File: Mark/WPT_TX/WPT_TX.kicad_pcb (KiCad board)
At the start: 4 copper layers, 102 x 44 mm, 119 parts, among them J1 Conn_01x01, J10 Conn_01x01, J2 Conn_01x01, J3 Conn_Coaxial, J4 Conn_Coaxial, J5 Conn_Coaxial, J6 Conn_02x05_Odd_Even, J7 Conn_01x03, J8 Conn_01x04, J9 Conn_01x01, Q1 NMOS, Q2 NMOS, Q3 NMOS, Q4 NMOS, U1 INA240A1D, U10 LM5106, U11 MCP2515-QFN20, U12 MCP2562-E-MF, U13 LM5106, U2 LM2937IMP-3.3, U3 LM2936-5.0, U4 LM2937IMP-12, U5 LMC6032, U6 CD4043BDR, U7 BTS6142DAUMA1, U8 SN74LVC1G14DBV, U9 ATSAMD21G16B-MFT, Y1 32.7680kHz, Y2 8MHz

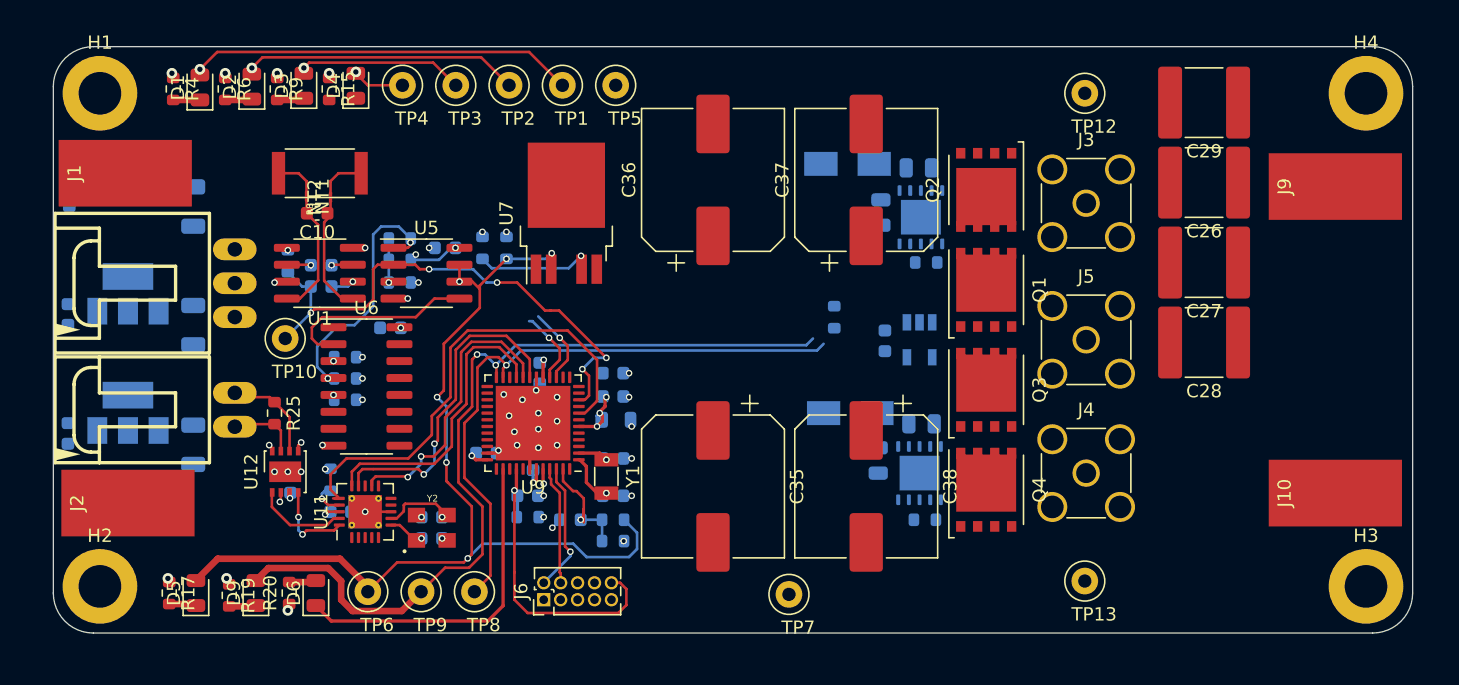
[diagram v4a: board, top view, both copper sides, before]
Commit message: Routing Final
- Finished all routing, should work out fine.
- All that's left is silkscreen
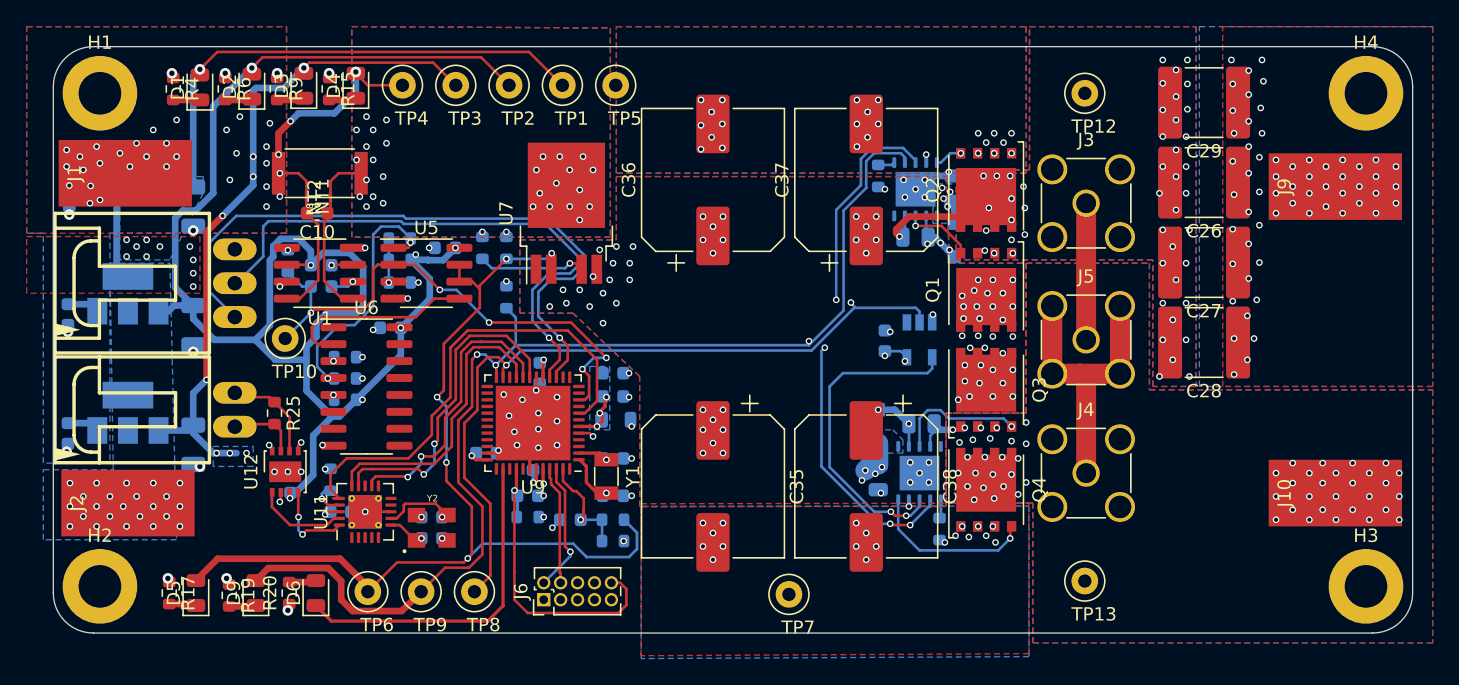
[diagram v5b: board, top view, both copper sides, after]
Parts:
- D7, D8: footprint Diodes_SMD:D_SMA -> Diode_SMD:D_SOD-323_HandSoldering
- moved R22 24.6 mm to (134.0, 112.3), turned to 270 degrees
- moved D7 9.82 mm to (167.6, 108.0), turned to 90 degrees
- moved R21 7.43 mm to (161.9, 103.2), turned to 90 degrees
- moved C21 5.79 mm to (167.6, 104.2), turned to 90 degrees
- moved C24 5.21 mm to (164.7, 107.8), turned to 180 degrees
- moved D8 2.33 mm to (161.9, 122.0), turned to 270 degrees
- moved U10 2.14 mm to (164.7, 104.2), turned to 90 degrees
- moved R24 1.30 mm to (166.5, 129.7), turned to 90 degrees
- moved C30 1.25 mm to (161.9, 125.8)
- turned Q1 to 270 degrees
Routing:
- net +12V: track 12.7 -> 145.9 mm, vias 1 -> 16
- net +5V: track 28.9 -> 119.0 mm
- net /HBridge_EN: track 64.9 -> 108.5 mm, vias 2 -> 6
- net /UART_TX: track 5.84 -> 49.3 mm
- net /UART_RX: track 5.62 -> 42.7 mm
- net /HBridge_PWM: track 46.8 -> 74.0 mm, vias 1 -> 3
- net /HS_2: track 0.00 -> 26.3 mm, vias 0 -> 52
- net /~HBridge_PWM~: track 0.00 -> 24.2 mm, vias 0 -> 2
- net GND: track 31.7 -> 52.4 mm, vias 46 -> 137
- net /HS_1: track 0.00 -> 20.6 mm, vias 0 -> 47
- net +24V: track 7.12 -> 25.9 mm, vias 1 -> 33
- net +3V3: track 38.0 -> 52.3 mm, vias 10 -> 22
- net /GATE4: track 0.00 -> 12.6 mm, vias 0 -> 1
- net /GATE2: track 0.00 -> 9.78 mm, vias 0 -> 1
- net /HD: track 0.00 -> 9.14 mm, vias 0 -> 73
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- added copper zone on B.Cu, net (none)
- added copper zone on B.Cu, net +12V
- added copper zone on B.Cu, net +24V
- added copper zone on F.Cu, net +24V
- added copper zone on B.Cu, net +3V3
- added copper zone on F.Cu, net +3V3
- added copper zone on In2.Cu, net +3V3
- added copper zone on B.Cu, net /3V3_Filt
- added copper zone on B.Cu, net /HD
- added copper zone on F.Cu, net /HD
- added copper zone on B.Cu, net /HS_1
- added copper zone on F.Cu, net /HS_1
- added copper zone on In2.Cu, net /HS_1
- added copper zone on B.Cu, net /HS_2
- added copper zone on F.Cu, net /HS_2
- added copper zone on In2.Cu, net /HS_2
- added copper zone on B.Cu, net GND
- added copper zone on F.Cu, net GND
- added copper zone on In1.Cu, net GND
- added copper zone on B.Cu, net Net-(C26-Pad1)
- added copper zone on F.Cu, net Net-(C26-Pad1)
- added copper zone on In2.Cu, net Net-(C26-Pad1)
- added copper zone on B.Cu, net Net-(NT2-Pad2)
- added copper zone on F.Cu, net Net-(NT2-Pad2)
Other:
- rule via_min_size: 0.4 -> 0.3

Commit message: Silkscreen & Touchups
- Board is finished!
- Fixed up silkscreen and some placement, looks good.
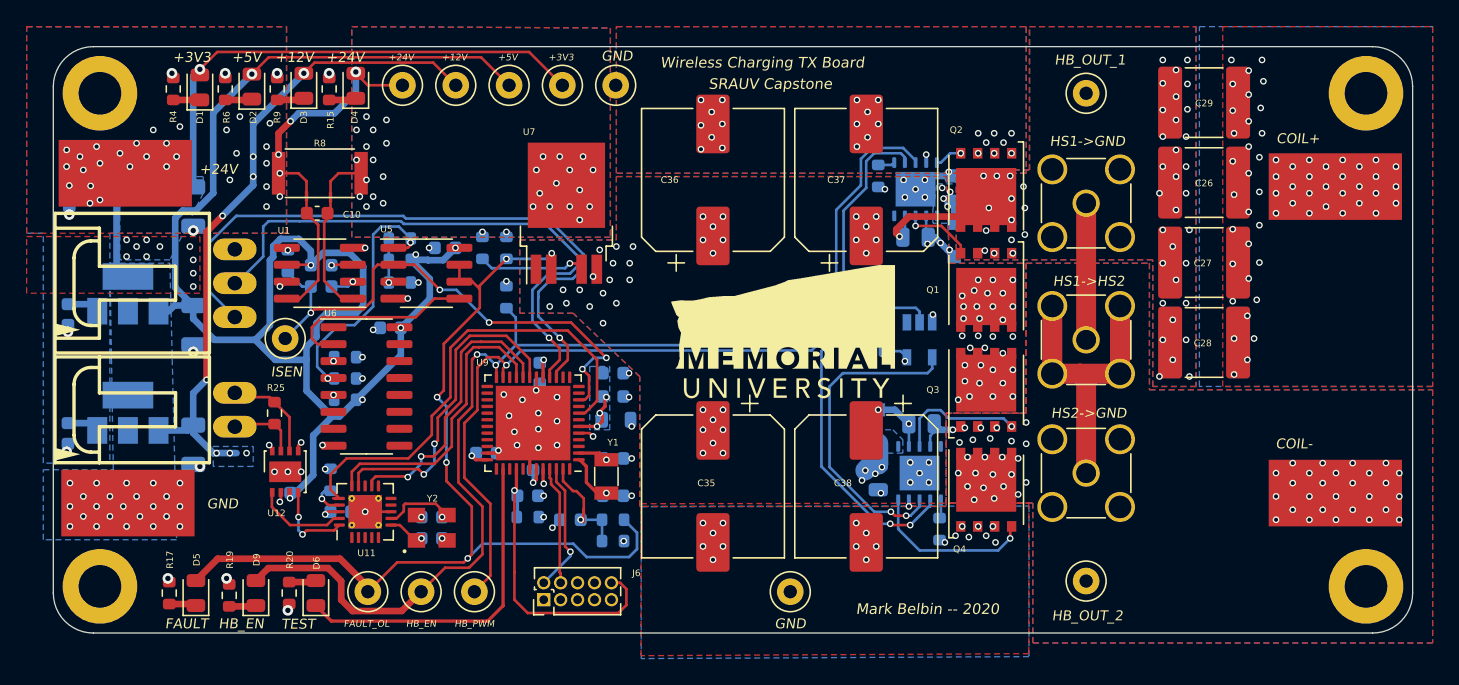
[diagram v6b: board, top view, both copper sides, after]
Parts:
- added U14: Munlogo, WPT_TX:MUNLOGO, F.Cu at (145.2, 121.0)
- moved TP7 0.22 mm to (155.3, 134.4)
- moved TP12 0.10 mm to (177.5, 97.0)
- moved TP13 0.10 mm to (177.5, 133.6)
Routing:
- net +12V: track 145.9 -> 144.0 mm
- net +5V: track 119.0 -> 118.3 mm
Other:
- board text added: "+12V"
- board text added: "+24V"
- board text added: "+3V3"
- board text added: "+5V"
- board text added: "COIL+"
- board text added: "COIL-"
- board text added: "FAULT"
- board text added: "FAULT_OL"
- board text added: "GND"
- board text added: "HB_EN"
- board text added: "HB_OUT_1"
- board text added: "HB_OUT_2"
- board text added: "HB_PWM"
- board text added: "HS1->GND"
- board text added: "HS1->HS2"
- board text added: "HS2->GND"
- board text added: "ISEN"
- board text added: "Mark Belbin -- 2020"
- board text added: "SRAUV Capstone"
- board text added: "TEST"
- board text added: "Wireless Charging TX Board"

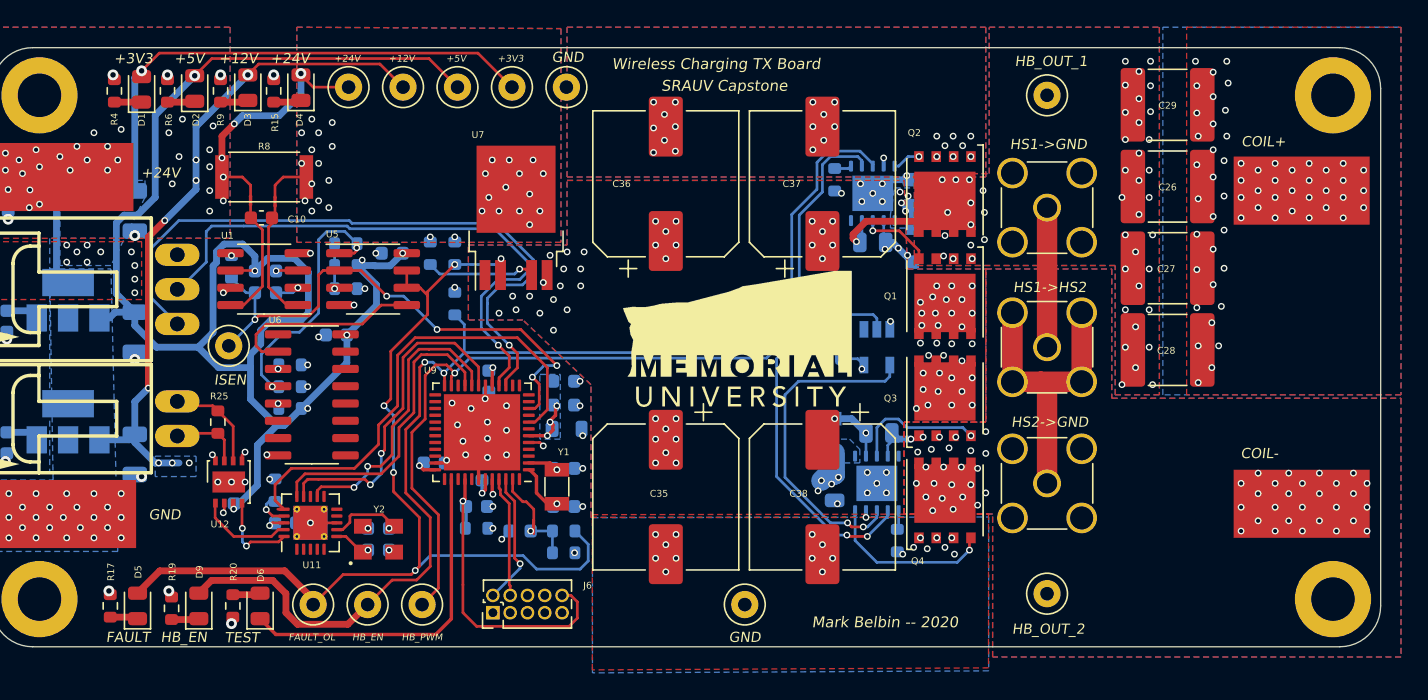
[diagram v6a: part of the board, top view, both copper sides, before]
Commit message: Updated TX
- Changed OL detector to a non inverting schmitt trigger.
- Updated routing, added more vias
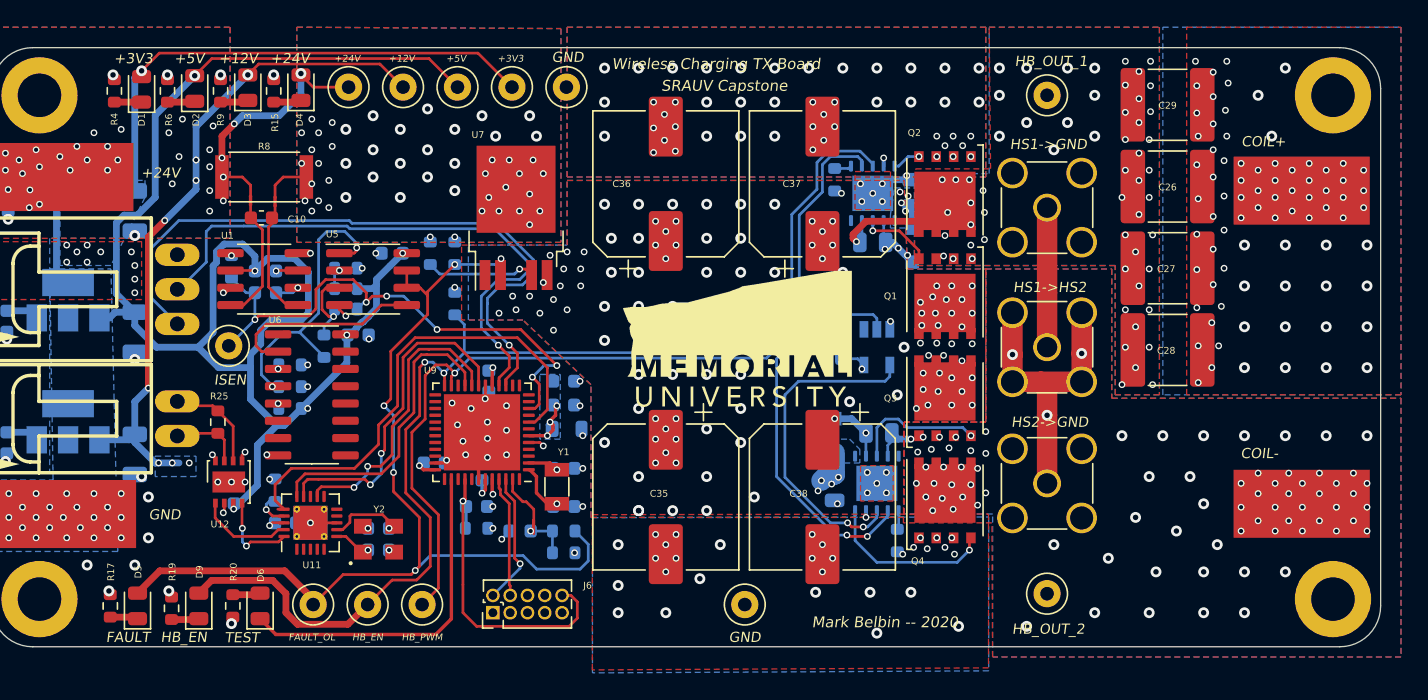
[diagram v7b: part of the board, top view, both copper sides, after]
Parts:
- added R26: 10k, Resistor_SMD:R_0603_1608Metric, B.Cu at (124.4, 115.4)
- R2: value 79.6k -> 10k
- R3: value 10k -> 12k
- R5: value 79.6k -> 1k
- moved R5 4.80 mm to (126.0, 112.7)
- moved R2 1.70 mm to (126.0, 111.2)
- moved C11 1.60 mm to (126.9, 114.6), turned to 0 degrees
- moved R3 1.50 mm to (126.0, 109.7)
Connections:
- R2 pad 1: Net-(R2-Pad1) -> /VREF
- R3 pad 2: Net-(R2-Pad1) -> /VREF
- R5 pad 1: Net-(R2-Pad1) -> Net-(R26-Pad2)
- R5 pad 2: Net-(R5-Pad2) -> /ISEN
- R7 pad 2: Net-(R5-Pad2) -> Net-(R26-Pad1)
- U5 pad 1: Net-(R5-Pad2) -> Net-(R26-Pad1)
- U5 pad 2: /ISEN -> /VREF
- U5 pad 3: Net-(R2-Pad1) -> Net-(R26-Pad2)
- U6 pad 4: Net-(R5-Pad2) -> Net-(R26-Pad1)
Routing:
- net Net-(R26-Pad1): track 0.00 -> 22.8 mm, vias 0 -> 2
- net Net-(R5-Pad2): track 20.2 -> 0.00 mm, vias 2 -> 0
- net Net-(R26-Pad2): track 0.00 -> 5.99 mm, vias 0 -> 1
- net Net-(R2-Pad1): track 3.68 -> 0.00 mm, vias 1 -> 0
- net /VREF: track 0.00 -> 1.92 mm, vias 0 -> 1
- net +5V: track 118.3 -> 116.6 mm, vias 7 -> 6
- net /ISEN: track 40.0 -> 40.6 mm, vias 5 -> 6
- net GND: track 52.4 -> 51.9 mm, vias 137 -> 176
- net Net-(NT2-Pad2): vias 28 -> 47
- net Net-(C26-Pad1): vias 59 -> 78
- net /HS_2: vias 52 -> 79
- net /HS_1: vias 47 -> 58
- net /HD: vias 73 -> 117
- net +3V3: vias 22 -> 23
- removed copper zone on B.Cu, net (none)

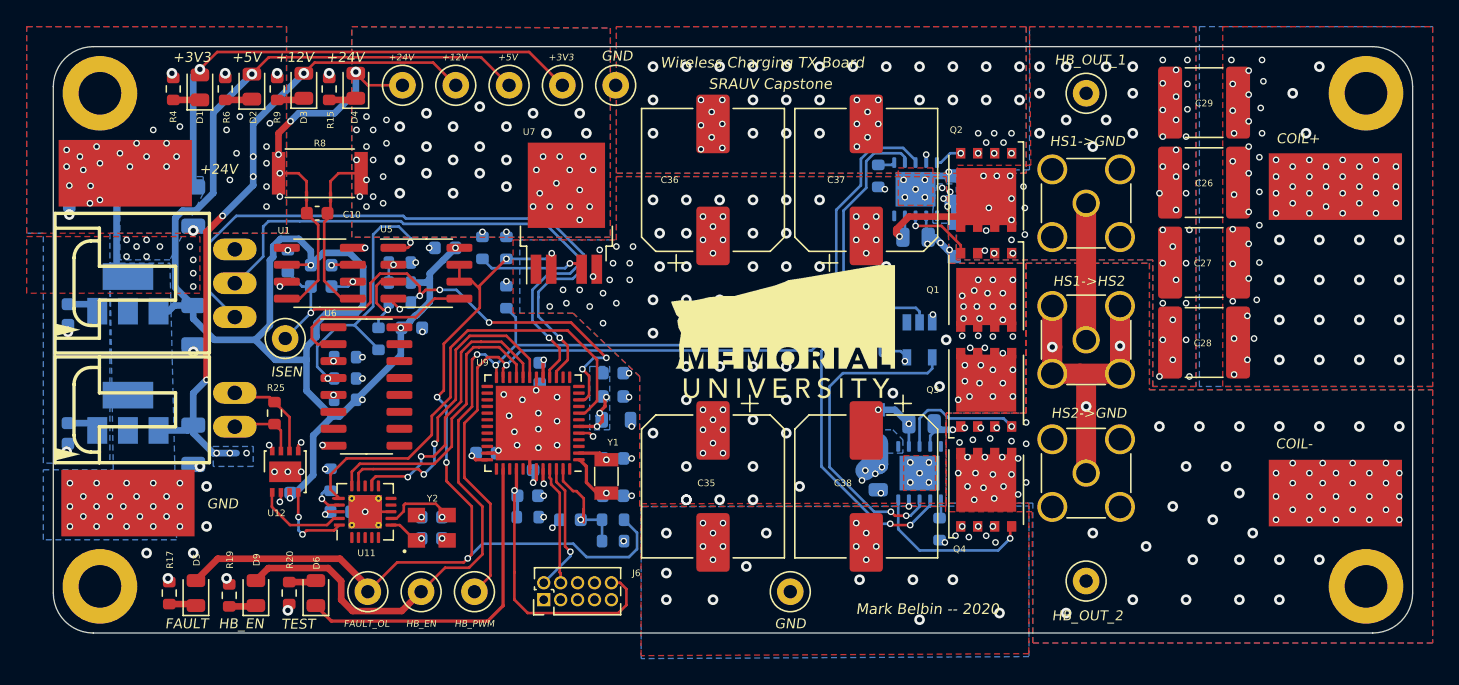
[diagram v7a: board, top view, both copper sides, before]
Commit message: Gerbers
- Generated gerbers
- Changed TX board size to 45x100mm to match RX board.
- Ordered PCBs like the impaitent bastard I am
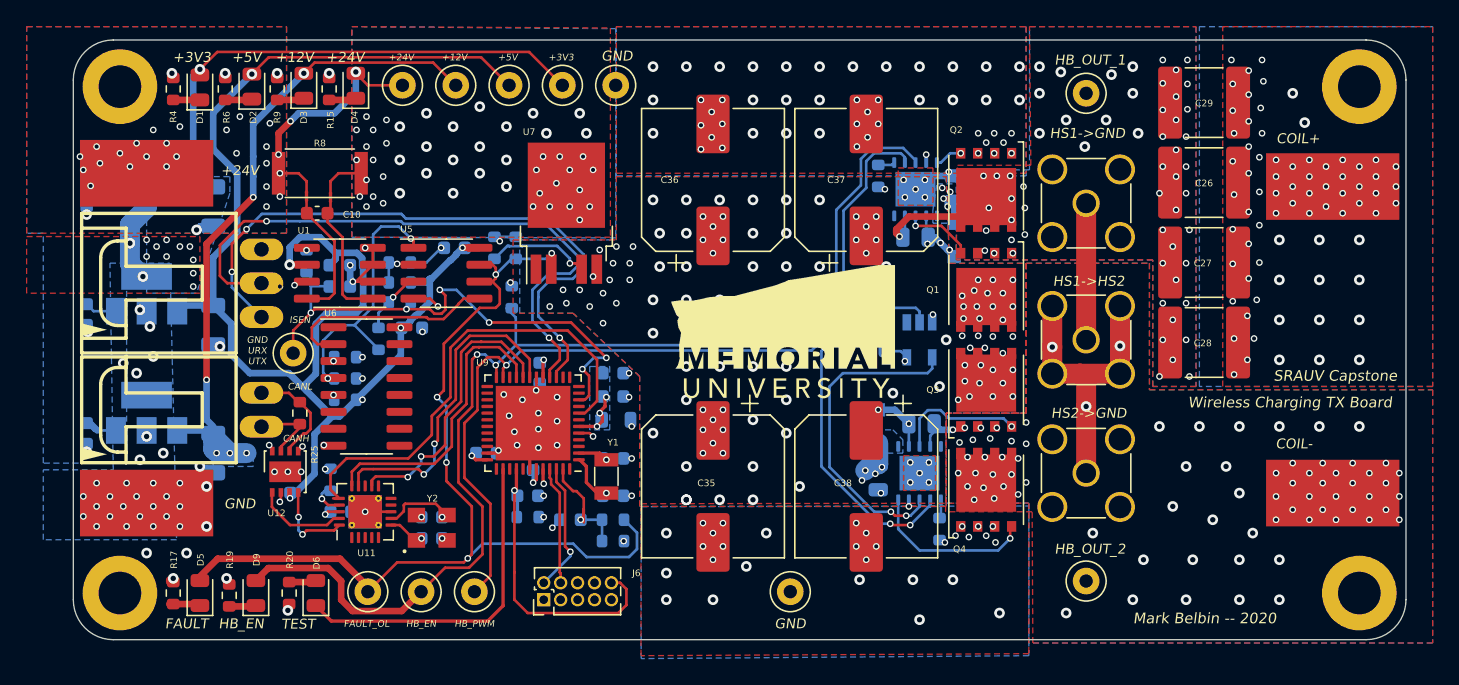
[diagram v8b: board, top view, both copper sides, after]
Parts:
- moved J7 2.00 mm to (108.0, 111.2)
- moved J8 2.00 mm to (108.0, 120.8)
- moved R25 1.90 mm to (118.5, 121.0)
- moved C8 1.62 mm to (112.0, 124.0)
- moved J1 1.60 mm to (107.0, 103.0)
- moved H1 1.58 mm to (105.0, 96.5)
- moved H2 1.58 mm to (105.0, 134.5)
- moved C6 1.50 mm to (112.0, 105.5)
- moved C7 1.50 mm to (112.0, 114.4)
- moved U1 1.50 mm to (121.5, 110.5)
- moved U5 1.50 mm to (129.5, 110.5)
- moved C2 1.40 mm to (102.5, 113.6)
- moved C3 1.40 mm to (102.5, 122.5)
- moved C4 1.40 mm to (121.5, 109.9)
- moved C9 1.40 mm to (121.5, 111.5)
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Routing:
- net GND: track 51.9 -> 61.8 mm, vias 176 -> 181
- net +12V: track 144.0 -> 150.7 mm, vias 16 -> 14
- net +5V: track 116.6 -> 111.3 mm
- net /UART_RX: track 42.7 -> 47.1 mm, vias 1 -> 3
- net /VREF: track 1.92 -> 3.60 mm
- net /FAULT_OL_SR: track 14.6 -> 16.2 mm
- net +3V3: track 52.3 -> 50.8 mm
- net /UART_TX: track 49.3 -> 47.8 mm, vias 1 -> 3
- net /I_IN-: track 8.85 -> 10.4 mm
- net Net-(R26-Pad1): track 22.8 -> 21.6 mm
- net /CANL: track 7.41 -> 8.48 mm
- net +24V: track 25.9 -> 24.9 mm, vias 33 -> 27
- net /CANH: track 5.28 -> 6.25 mm
- net /I_IN+: track 9.26 -> 10.1 mm
- net /FAULT_OL: track 73.4 -> 74.1 mm
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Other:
- board size 102 x 44 mm -> 100 x 45 mm
- board text added: "CANH"
- board text added: "CANL"
- board text added: "URX"
- board text added: "UTX"
